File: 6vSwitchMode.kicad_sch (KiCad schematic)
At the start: 29 parts, among them IC3 TPS40192DRCT-TPS40192DRCT, Q2 BUK9M17-30EX / BUK7M10-40E, Q3 BUK9M17-30EX / BUK7M10-40E

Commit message: Addressing the issues with the sample version, Updating the bom to source all the correct components from the JLCPCB supply
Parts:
- Q2, Q3: value BUK9M17-30EX / BUK7M10-40E -> AON7262E; footprint Package_SON:VSON-8_3.3x3.3mm_P0.65mm_NexFET -> 2450AT43F0100:DFN-8
- R40, TP10, TP11, TP9: now left out of the parts list
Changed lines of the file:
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@@
   )
   (symbol (lib_id "Connector:TestPoint") (at 242.57 36.83 0) (unit 1)
-    (in_bom yes) (on_board yes)
+    (in_bom no) (on_board yes)
     (property "Reference" "TP11" (id 0) (at 244.0432 33.8328 0)
       (effects (font (size 1.27 1.27)) (justify left))
@@
   )
   (symbol (lib_id "Connector:TestPoint") (at 228.6 36.83 0) (unit 1)
-    (in_bom yes) (on_board yes)
+    (in_bom no) (on_board yes)
     (property "Reference" "TP10" (id 0) (at 230.0732 33.8328 0)
       (effects (font (size 1.27 1.27)) (justify left))
@@
   )
   (symbol (lib_id "Connector:TestPoint") (at 214.63 36.83 0) (unit 1)
-    (in_bom yes) (on_board yes)
+    (in_bom no) (on_board yes)
     (property "Reference" "TP9" (id 0) (at 216.1032 33.8328 0)
       (effects (font (size 1.27 1.27)) (justify left))
@@
   )
   (symbol (lib_id "Device:R") (at 115.57 107.95 0) (unit 1)
-    (in_bom yes) (on_board yes)
+    (in_bom no) (on_board yes)
     (property "Reference" "R40" (id 0) (at 117.348 106.7816 0)
       (effects (font (size 1.27 1.27)) (justify left))
@@
       (effects (font (size 1.27 1.27)) (justify left))
     )
-    (property "Value" "BUK9M17-30EX / BUK7M10-40E" (id 1) (at 177.9524 93.853 0)
-      (effects (font (size 1.27 1.27)) (justify left))
-    )
-    (property "Footprint" "Package_SON:VSON-8_3.3x3.3mm_P0.65mm_NexFET" (id 2) (at 177.8 94.615 0)
+    (property "Value" "AON7262E" (id 1) (at 177.9524 93.853 0)
+      (effects (font (size 1.27 1.27)) (justify left))
+    )
+    (property "Footprint" "2450AT43F0100:DFN-8" (id 2) (at 177.8 94.615 0)
       (effects (font (size 1.27 1.27) italic) (justify left) hide)
     )
@@
       (effects (font (size 1.27 1.27)) (justify left))
     )
-    (property "Value" "BUK9M17-30EX / BUK7M10-40E" (id 1) (at 177.9524 74.803 0)
-      (effects (font (size 1.27 1.27)) (justify left))
-    )
-    (property "Footprint" "Package_SON:VSON-8_3.3x3.3mm_P0.65mm_NexFET" (id 2) (at 177.8 75.565 0)
+    (property "Value" "AON7262E" (id 1) (at 177.9524 74.803 0)
+      (effects (font (size 1.27 1.27)) (justify left))
+    )
+    (property "Footprint" "2450AT43F0100:DFN-8" (id 2) (at 177.8 75.565 0)
       (effects (font (size 1.27 1.27) italic) (justify left) hide)
     )

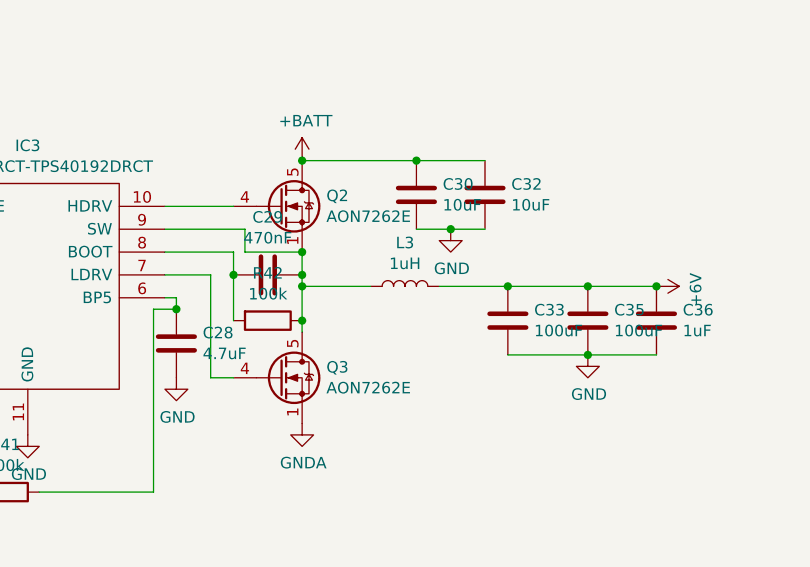
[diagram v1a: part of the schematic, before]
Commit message: Adding usb c pd negotiation for battery charging
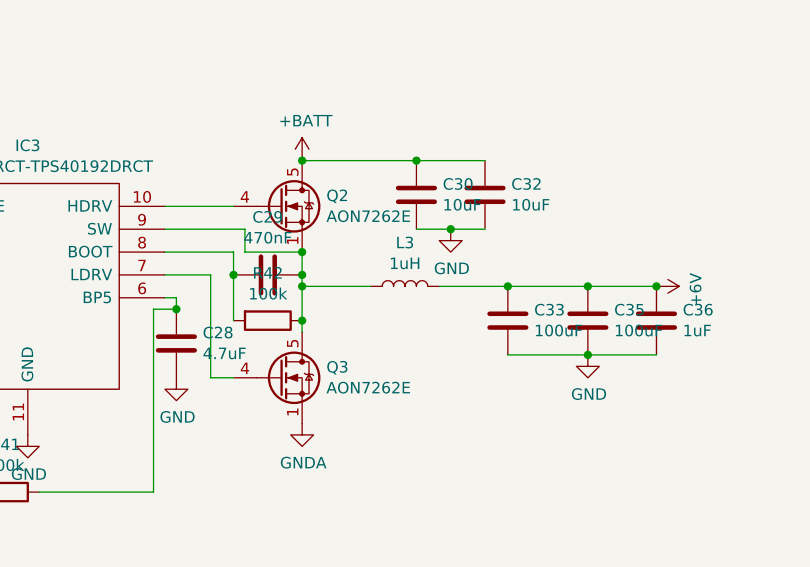
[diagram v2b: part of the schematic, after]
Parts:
- Q2, Q3: footprint 2450AT43F0100:DFN-8 -> Package_TO_SOT_SMD:LFPAK33
